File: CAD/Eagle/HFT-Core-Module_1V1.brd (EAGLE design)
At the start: 96.5 x 96.5 mm, 526 parts, among them Q0321 ABS07-32.768KHZ, Q1321 ABS07-32.768KHZ, Q2211 ABM3B-32.0000MHZ, Q2311 ABM3B-16.0000MHZ, T1051 MMBT2222, T1111 MMBT2222, T1121 MMBT2222, T1131 MMBT2222, U0111 STM32L4Z_144PIN_SMPS, U0521 PCAL6416APW, U0621 PCAL6416APW, U0711 IS25LP032D, U0721 IS25LP032D, U0801 CAT24C64, U0911 ZIO_EINK_1IN54, U1001 MIDAS_MCCOG21605B6W-FPTLWI, U1301 BNO085, U1401 BME680, U1501 LM4120IM5-3.0, U1511 MAX5217, U1531 CFPT-141-20MHZ, U1541 OPA354, U1542 LPV811, U1601 Si5338, U1651 TS5A23166, U1701 PCM1863, U1801 WM8523, U1901 SIM868, U2001 74LVC4245A, U2101 74LVC4245A, U2201 SX1262, U2271 PE4259, U2301 AX5243, U2401 LM53603-Q1, U2501 BQ24193, U2541 LPV811, U2601 BQ25570, U2681 TS5A23166, U2701 TPS62051, U2751 MCP4661-104E-MS, U2801 TS5A23166, U2901 TS5A23166, U3001 TS5A23166, U3101 TS5A23166, U3391 TS5A23166, U3392 TDK B4310, X1201 TTE_EN11-HSM, X1951 MICROSIM-8P_SDCARD-8P_MOLEX-1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, X2411 WIRE-TO-BOARD_5MM08_1X02, X2551 JST_S3B-XH-A, X2601 WIRE-TO-BOARD_5MM08_1X02, X3201 MOLEX 105017-0001, X3301 SMA_SMT_AMPHENOL-901-143, X3311 SAMTEC SMA-J-P-H-RA-TH1, X3371 SMA_SMT_AMPHENOL-901-143, SAM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, X3381 SMA_SMT_AMPHENOL-901-143, SAM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, X3391 SMA_SMT_AMPHENOL-901-143, SAM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, X3401 CUI SJ1-3535NS, X3411 CUI SJ1-3535NS, X3511 2X20/90_1MM27_HARWIN_M50-3202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, X3512 2X20/90_1MM27_HARWIN_M50-3202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, X3531 2X20/90_1MM27_HARWIN_M50-3202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, X3532 2X20/90_1MM27_HARWIN_M50-3202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

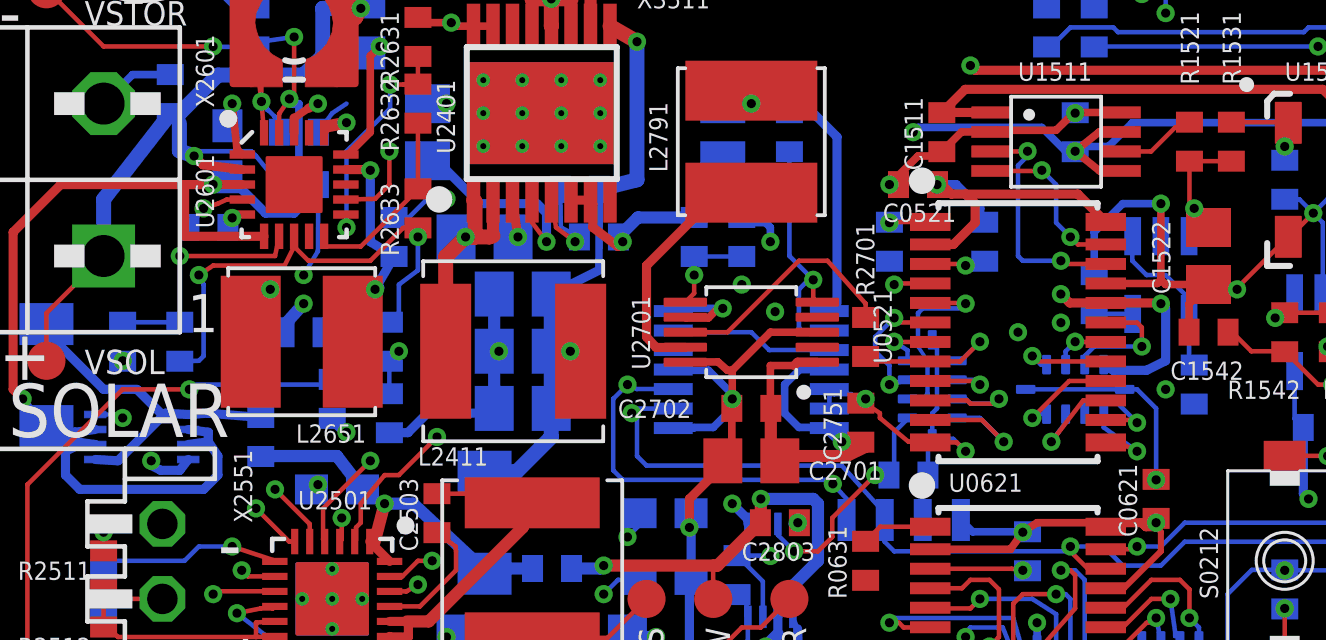
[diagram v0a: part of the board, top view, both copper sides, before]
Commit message: HW_1V1 - CAD/Eagle - DRC findings solved
Signed-off-by: Ulrich Habel <espero7757@gmx.net>
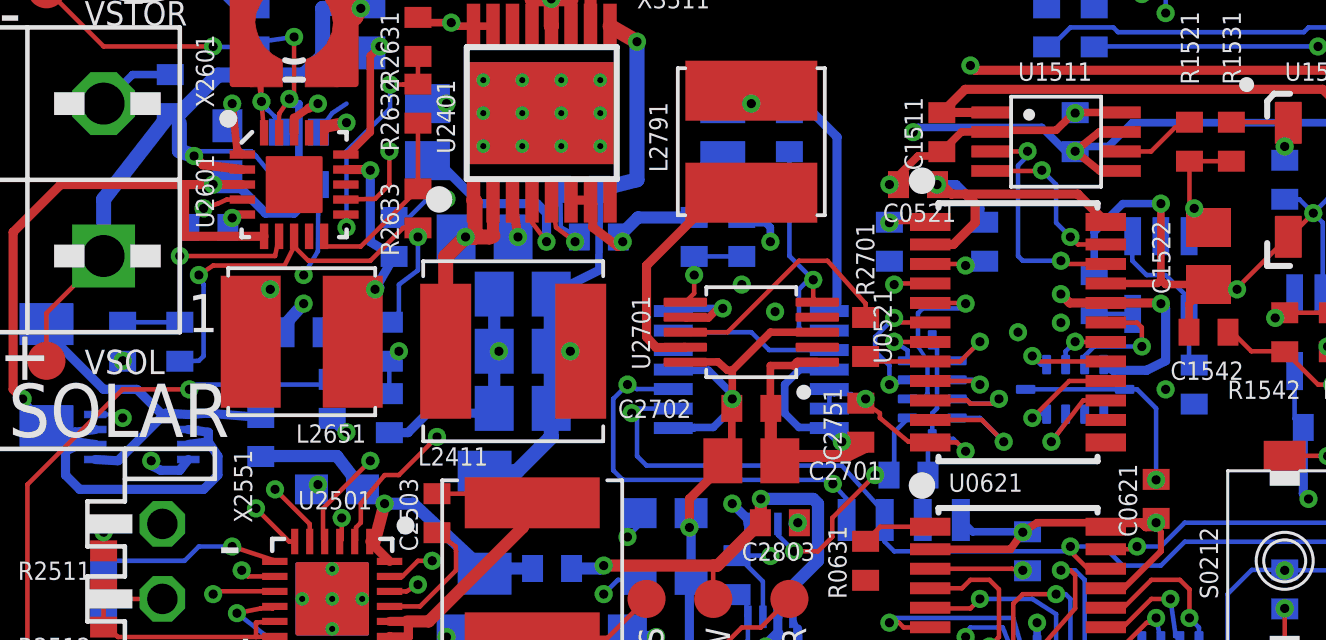
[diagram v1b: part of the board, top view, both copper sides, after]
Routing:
- net PEXPA_P1_1_R: track 3.57 -> 0.00 mm, vias 1 -> 0
- net PEXPA_P1_0_R: track 2.92 -> 0.00 mm, vias 1 -> 0
- net BQ_VSTOR: track 53.9 -> 53.2 mm
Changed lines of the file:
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@@
 <layer number="18" name="Vias" color="2" fill="1" visible="yes" active="yes"/>
 <layer number="19" name="Unrouted" color="6" fill="1" visible="yes" active="yes"/>
-<layer number="20" name="Dimension" color="5" fill="1" visible="no" active="yes"/>
+<layer number="20" name="Dimension" color="5" fill="1" visible="yes" active="yes"/>
 <layer number="21" name="tPlace" color="7" fill="1" visible="no" active="yes"/>
 <layer number="22" name="bPlace" color="7" fill="1" visible="no" active="yes"/>
-<layer number="23" name="tOrigins" color="15" fill="1" visible="no" active="yes"/>
-<layer number="24" name="bOrigins" color="15" fill="1" visible="no" active="yes"/>
+<layer number="23" name="tOrigins" color="15" fill="1" visible="yes" active="yes"/>
+<layer number="24" name="bOrigins" color="15" fill="1" visible="yes" active="yes"/>
 <layer number="25" name="tNames" color="7" fill="1" visible="no" active="yes"/>
 <layer number="26" name="bNames" color="7" fill="1" visible="no" active="yes"/>
@@
 <layer number="43" name="vRestrict" color="2" fill="10" visible="no" active="yes"/>
 <layer number="44" name="Drills" color="7" fill="1" visible="no" active="yes"/>
-<layer number="45" name="Holes" color="7" fill="1" visible="no" active="yes"/>
-<layer number="46" name="Milling" color="3" fill="1" visible="no" active="yes"/>
+<layer number="45" name="Holes" color="7" fill="1" visible="yes" active="yes"/>
+<layer number="46" name="Milling" color="3" fill="1" visible="yes" active="yes"/>
 <layer number="47" name="Measures" color="13" fill="1" visible="no" active="yes"/>
 <layer number="48" name="Document" color="7" fill="1" visible="no" active="yes"/>
-<layer number="49" name="Reference" color="7" fill="1" visible="no" active="yes"/>
+<layer number="49" name="Reference" color="7" fill="1" visible="yes" active="yes"/>
 <layer number="50" name="dxf" color="7" fill="1" visible="no" active="no"/>
 <layer number="51" name="tDocu" color="14" fill="1" visible="no" active="yes"/>
@@
 <wire x1="8.04" y1="82.55" x2="7.9375" y2="82.6525" width="0.3048" layer="16"/>
 <wire x1="9.16" y1="80.66625" x2="6.4875" y2="80.66625" width="0.3048" layer="1"/>
-<wire x1="6.50875" y1="80.80375" x2="6.50875" y2="81.28" width="0.3048" layer="1"/>
-<wire x1="6.50875" y1="81.28" x2="6.50875" y2="82.39125" width="0.3048" layer="1"/>
+<wire x1="6.50875" y1="80.80375" x2="6.50875" y2="82.39125" width="0.3048" layer="1"/>
 <wire x1="6.50875" y1="82.39125" x2="7.46125" y2="82.39125" width="0.3048" layer="1"/>
 <wire x1="6.50875" y1="80.80375" x2="6.4875" y2="80.94125" width="0.3048" layer="1"/>
@@
 <wire x1="1.11125" y1="75.2475" x2="1.7" y2="74.34125" width="0.3048" layer="16"/>
 <wire x1="1.7" y1="74.34125" x2="1.905" y2="74.34125" width="0.3048" layer="16"/>
-<wire x1="6.4875" y1="80.66625" x2="6.50875" y2="80.66625" width="0.1524" layer="1"/>
-<wire x1="6.50875" y1="80.66625" x2="6.50875" y2="81.28" width="0.1524" layer="1"/>
+<wire x1="6.50875" y1="80.80375" x2="6.4875" y2="80.66625" width="0" layer="19" extent="1-1"/>
 </signal>
 <signal name="BQ_LBUCK">
@@
 <contactref element="R0581" pad="3"/>
 <contactref element="U0521" pad="5"/>
-<wire x1="30.6075" y1="75.2475" x2="31.115" y2="75.2475" width="0.1524" layer="16"/>
+<wire x1="30.63875" y1="75.2475" x2="31.115" y2="75.2475" width="0.1524" layer="16"/>
 <wire x1="31.115" y1="75.2475" x2="31.27375" y2="75.40625" width="0.1524" layer="16"/>
 <wire x1="31.27375" y1="75.40625" x2="31.27375" y2="76.5175" width="0.1524" layer="16"/>
@@
 <wire x1="32.22625" y1="54.9275" x2="32.0675" y2="54.76875" width="0.1524" layer="15"/>
 <wire x1="32.0675" y1="54.76875" x2="32.0675" y2="53.49875" width="0.1524" layer="15"/>
+<wire x1="30.63875" y1="75.2475" x2="30.6075" y2="75.2475" width="0" layer="19" extent="16-16"/>
 </signal>
 <signal name="PEXPA_P0_2_R">
@@
 <contactref element="R0591" pad="2"/>
 <contactref element="U0521" pad="13"/>
-<via x="38.25875" y="73.50125" extent="1-16" drill="0.3048"/>
-<wire x1="37.215" y1="73.795" x2="37.6475" y2="73.795" width="0.1524" layer="1"/>
-<wire x1="37.6475" y1="73.795" x2="38.25875" y2="73.50125" width="0.1524" layer="1"/>
-<wire x1="37.1475" y1="74.74" x2="37.1475" y2="74.295" width="0.1524" layer="16"/>
-<wire x1="37.1475" y1="74.295" x2="38.25875" y2="73.50125" width="0.1524" layer="16"/>
-<wire x1="45.9975" y1="42.295" x2="38.25875" y2="73.50125" width="0" layer="19" extent="1-1"/>
+<wire x1="37.215" y1="73.795" x2="37.1475" y2="74.74" width="0" layer="19" extent="1-16"/>
+<wire x1="45.9975" y1="42.295" x2="37.215" y2="73.795" width="0" layer="19" extent="1-1"/>
 </signal>
 <signal name="PEXPA_P1_1_R">
@@
 <contactref element="R0591" pad="3"/>
 <contactref element="U0521" pad="14"/>
-<via x="38.25875" y="74.45375" extent="1-16" drill="0.3048"/>
-<wire x1="37.215" y1="74.545" x2="38.1675" y2="74.545" width="0.1524" layer="1"/>
-<wire x1="38.1675" y1="74.545" x2="38.25875" y2="74.45375" width="0.1524" layer="1"/>
-<wire x1="36.5125" y1="74.74" x2="36.5125" y2="75.08875" width="0.1524" layer="16"/>
-<wire x1="36.5125" y1="75.08875" x2="36.67125" y2="75.2475" width="0.1524" layer="16"/>
-<wire x1="36.67125" y1="75.2475" x2="37.465" y2="75.2475" width="0.1524" layer="16"/>
-<wire x1="37.465" y1="75.2475" x2="38.25875" y2="74.45375" width="0.1524" layer="16"/>
-<wire x1="48.51" y1="40.9825" x2="38.25875" y2="74.45375" width="0" layer="19" extent="1-1"/>
+<wire x1="37.215" y1="74.545" x2="36.5125" y2="74.74" width="0" layer="19" extent="1-16"/>
+<wire x1="48.51" y1="40.9825" x2="37.215" y2="74.545" width="0" layer="19" extent="1-1"/>
 </signal>
 <signal name="PEXPA_P1_2_R">

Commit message: HW_1V1 - CAD/Eagle - some more wires routed in the west
Signed-off-by: Ulrich Habel <espero7757@gmx.net>
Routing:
- net PG4: track 6.16 -> 75.6 mm, vias 0 -> 4
- net +5V0: track 23.6 -> 80.9 mm
- net PF6: track 0.00 -> 43.6 mm, vias 0 -> 3
- net PC13: track 0.00 -> 37.1 mm, vias 0 -> 3
- net MCU_NRST: track 102.5 -> 102.8 mm, vias 3 -> 5

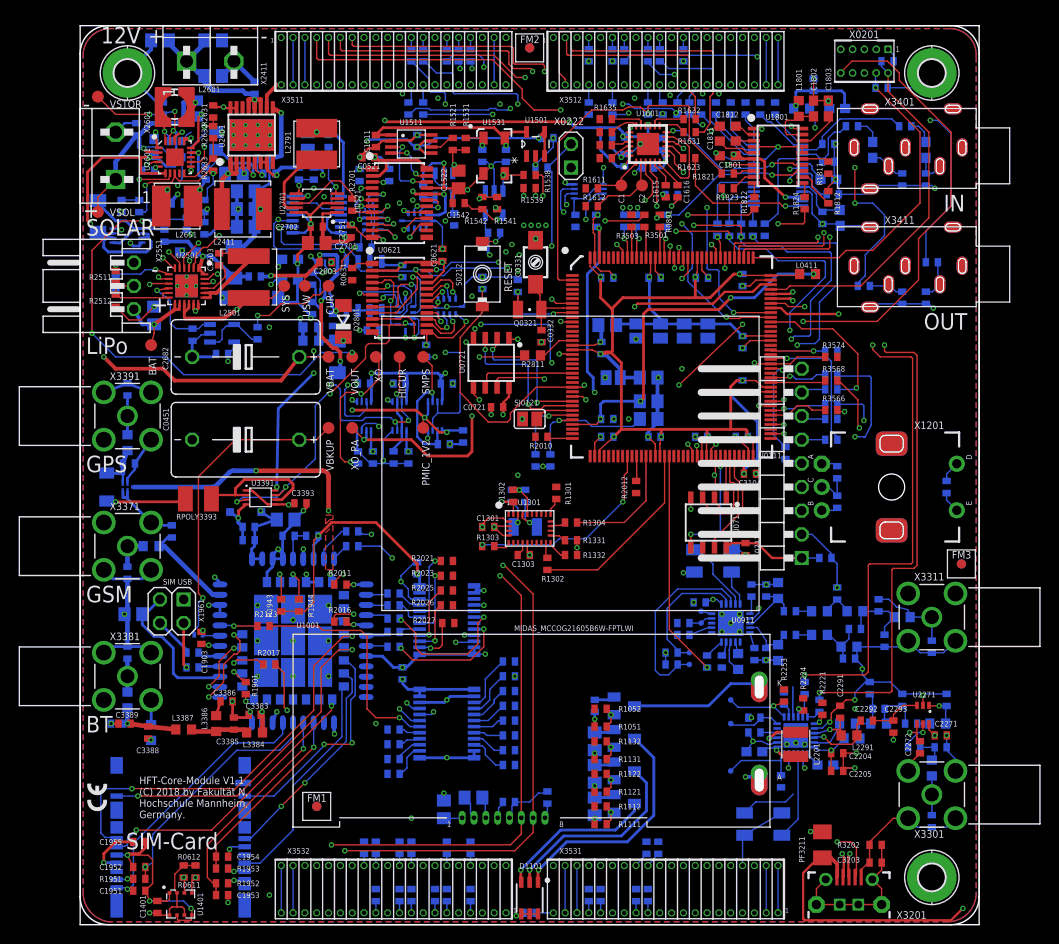
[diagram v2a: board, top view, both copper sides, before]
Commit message: HW_1V1 - CAD/Eagle - some routing in the south done
Signed-off-by: Ulrich Habel <espero7757@gmx.net>
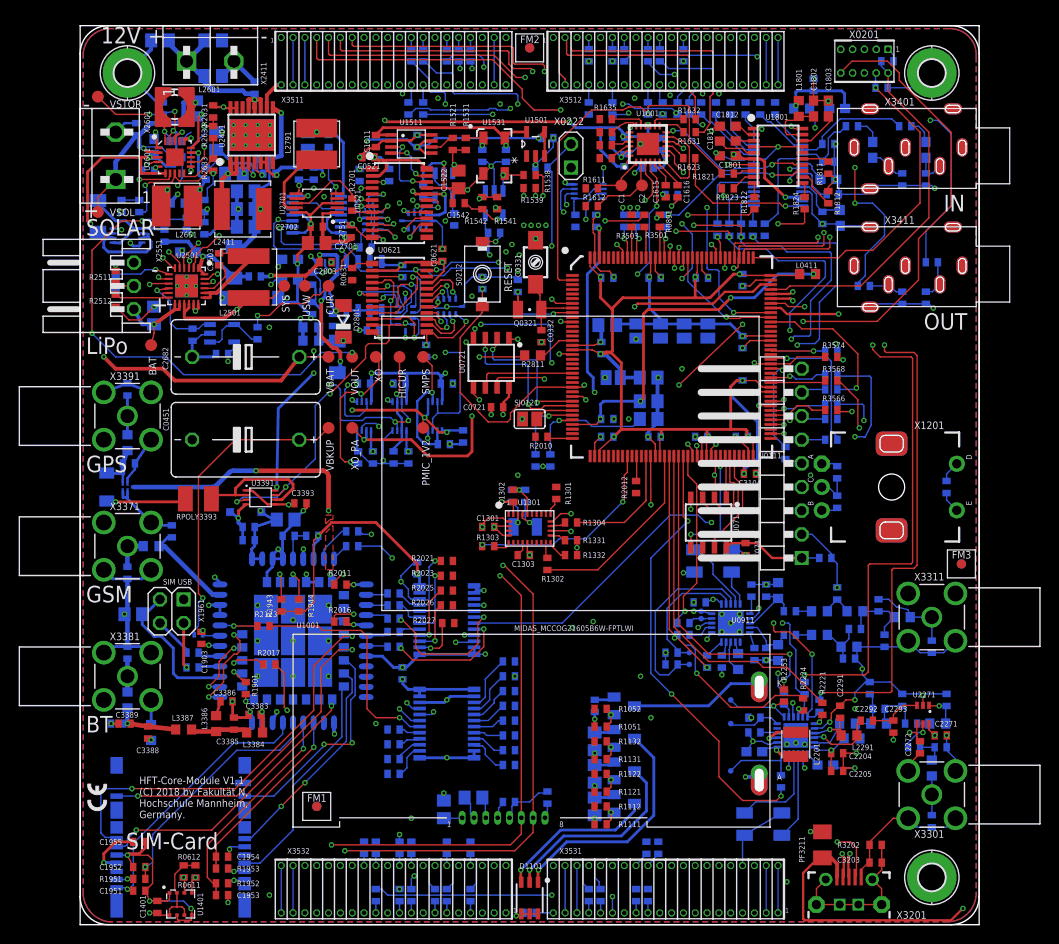
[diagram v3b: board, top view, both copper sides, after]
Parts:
- moved TP_AX_IRQ 0.48 mm to (66.7, 32.9)
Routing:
- net PB13: track 62.2 -> 151.1 mm, vias 5 -> 6
- net PE9: track 48.6 -> 133.1 mm, vias 4 -> 5
- net PE10: track 64.8 -> 147.6 mm, vias 3 -> 4
- net EVT_S_OUT: track 0.00 -> 81.3 mm, vias 0 -> 3
- net PE8: track 53.0 -> 129.5 mm, vias 3 -> 4
- net MCU_SPI3_SCK: track 1.51 -> 72.1 mm, vias 0 -> 5
- net MCU_SPI3_MOSI: track 2.46 -> 66.9 mm, vias 0 -> 4
- net MCU_LPUART_DTR_OUT_R: track 0.00 -> 63.6 mm, vias 0 -> 3
- net AX_8MHZ: track 5.01 -> 67.0 mm, vias 1 -> 4
- net PG1: track 0.00 -> 48.2 mm, vias 0 -> 3
- net PC11: track 11.7 -> 57.1 mm, vias 1 -> 4
- net PF12: track 23.0 -> 62.1 mm, vias 3 -> 6
- net PF15: track 0.00 -> 37.7 mm
- net PG0: track 0.00 -> 35.4 mm, vias 0 -> 2
- net PD8: track 0.00 -> 32.1 mm, vias 0 -> 2
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
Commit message: HW_1V1 - CAD/Eagle - more routing of the day done
Signed-off-by: Ulrich Habel <espero7757@gmx.net>
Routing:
- net PG9: track 70.0 -> 120.5 mm, vias 4 -> 5
- net PG12: track 70.8 -> 119.3 mm, vias 3 -> 4
- net PG11: track 64.1 -> 110.6 mm, vias 3 -> 4
- net PG10: track 68.9 -> 112.7 mm, vias 3 -> 4
- net PE8: track 129.5 -> 130.0 mm
